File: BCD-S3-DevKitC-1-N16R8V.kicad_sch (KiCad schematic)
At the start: 51 parts, among them J1 Conn_01x22, J2 Conn_01x22, Q1 SS8050, Q2 SS8050, SW1 BOOT, SW2 RESET, U1 ESP32-S3-WROOM-1, U2 AMS1117-3.3, U3 CH343P

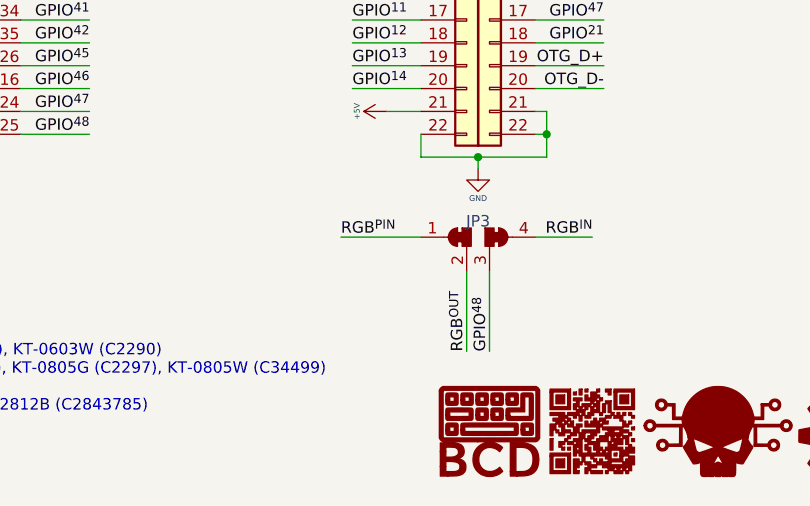
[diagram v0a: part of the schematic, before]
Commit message: Add help for RGB48 jumper. Fixed error in PCB for RGB48.
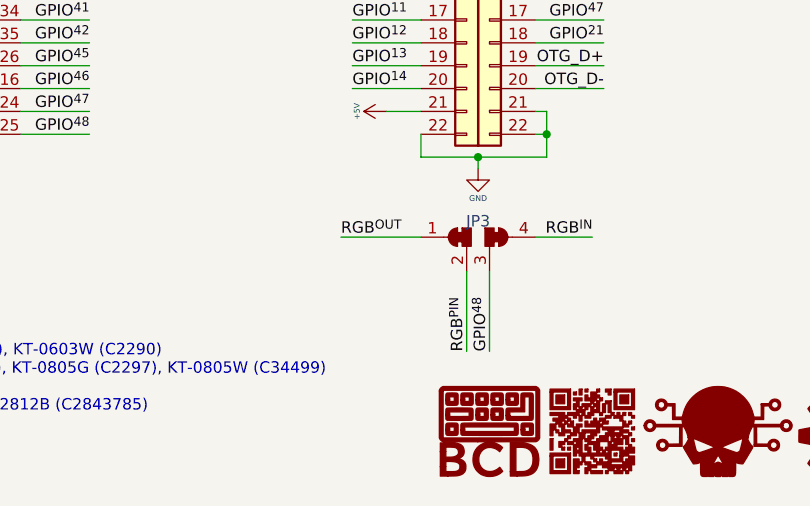
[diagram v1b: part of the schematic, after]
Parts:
- G2: footprint BeaupreCircuitDesign:BDC_QR_2.5mm -> BCD-S3-DevKitC-1-N16R8V:BCD-S3-DevKitC-1_5mm
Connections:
- net RGB^{OUT}: now also JP3.1 (A); no longer JP3.2 (C)
- net RGB^{PIN}: now also JP3.2 (C); no longer JP3.1 (A)
